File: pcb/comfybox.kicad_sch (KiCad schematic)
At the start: 20 parts, among them K1 SW_CHOC, K2 SW_CHOC, K3 SW_CHOC, K4 SW_CHOC, P1 SW_CHOC, P2 SW_CHOC, P3 SW_CHOC, P4 SW_CHOC

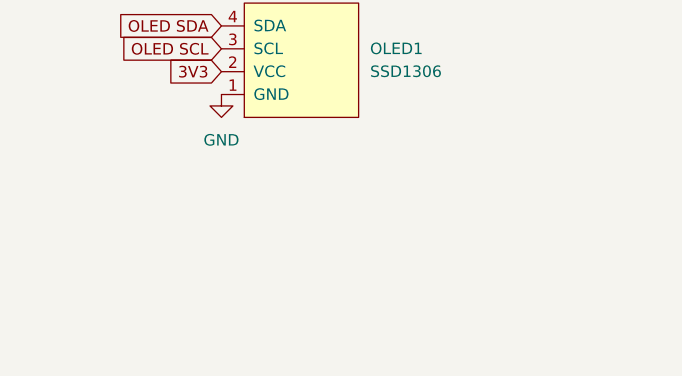
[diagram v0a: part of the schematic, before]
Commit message: add back oled
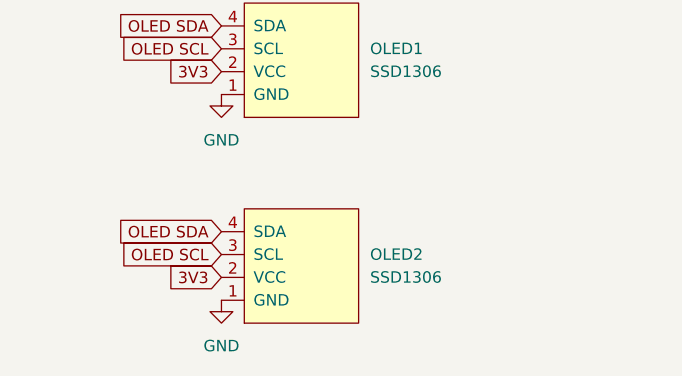
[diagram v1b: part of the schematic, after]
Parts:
- added OLED2: SSD1306, OLED:SSD1306-128x64_OLED, symbol SSD1306-128x64_OLED:SSD1306
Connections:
- net 3V3: now also OLED2.2 (VCC)
- net GND: now also OLED2.1 (GND)
- net OLED SCL: now also OLED2.3 (SCL)
- net OLED SDA: now also OLED2.4 (SDA)
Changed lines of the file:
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@@
+    )
+  )
+  (global_label "3V3" (shape input) (at 54.61 151.13 180) (fields_autoplaced)
+    (effects (font (size 1.27 1.27)) (justify right))
+    (property "Intersheetrefs" "${INTERSHEET_REFS}" (at 48.6893 151.2094 0)
+      (effects (font (size 1.27 1.27)) (justify right) hide)
     )
   )
@@
     )
   )
+  (global_label "OLED SCL" (shape input) (at 54.61 148.59 180) (fields_autoplaced)
+    (effects (font (size 1.27 1.27)) (justify right))
+    (property "Intersheetrefs" "${INTERSHEET_REFS}" (at 42.944 148.5106 0)
+      (effects (font (size 1.27 1.27)) (justify right) hide)
+    )
+  )
   (global_label "LEFT" (shape input) (at 115.57 72.39 270) (fields_autoplaced)
     (effects (font (size 1.27 1.27)) (justify right))
     (property "Intersheetrefs" "${INTERSHEET_REFS}" (at 115.4906 79.0364 90)
+      (effects (font (size 1.27 1.27)) (justify right) hide)
+    )
+  )
+  (global_label "OLED SDA" (shape input) (at 54.61 146.05 180) (fields_autoplaced)
+    (effects (font (size 1.27 1.27)) (justify right))
+    (property "Intersheetrefs" "${INTERSHEET_REFS}" (at 42.8836 145.9706 0)
       (effects (font (size 1.27 1.27)) (justify right) hide)
     )
@@
     )
   )
+  (symbol (lib_id "power:GND") (at 54.61 153.67 0) (unit 1)
+    (in_bom yes) (on_board yes) (dnp no) (fields_autoplaced)
+    (property "Reference" "#PWR03" (at 54.61 160.02 0)
+      (effects (font (size 1.27 1.27)) hide)
+    )
+    (property "Value" "GND" (at 54.61 158.75 0)
+      (effects (font (size 1.27 1.27)))
+    )
+    (property "Footprint" "" (at 54.61 153.67 0)
+      (effects (font (size 1.27 1.27)) hide)
+    )
+    (property "Datasheet" "" (at 54.61 153.67 0)
+      (effects (font (size 1.27 1.27)) hide)
+    )
+    (pin "1")
+    (instances
+      (project "comfybox"
+        (path "/9a77f188-2d2d-4d89-86c0-244b937205f9"
+          (reference "#PWR03") (unit 1)
+        )
+      )
+    )
+  )
   (symbol (lib_id "power:GND") (at 146.05 119.38 0) (unit 1)
     (in_bom yes) (on_board yes) (dnp no) (fields_autoplaced)
@@
         )
       )
+    )
+  )
+  (symbol (lib_id "SSD1306-128x64_OLED:SSD1306") (at 63.5 149.86 90) (unit 1)
+    (in_bom yes) (on_board yes) (dnp no) (fields_autoplaced)
+    (property "Reference" "OLED2" (at 71.12 148.5899 90)
+      (effects (font (size 1.27 1.27)) (justify right))
+    )
+    (property "Value" "SSD1306" (at 71.12 151.1299 90)
+      (effects (font (size 1.27 1.27)) (justify right))
+    )
+    (property "Footprint" "OLED:SSD1306-128x64_OLED" (at 57.15 149.86 0)
+      (effects (font (size 1.27 1.27)) hide)
+    )
+    (property "Datasheet" "" (at 57.15 149.86 0)
+      (effects (font (size 1.27 1.27)) hide)
+    )
+    (pin "1")
+    (pin "2")
+    (pin "3")
+    (pin "4")
+    (instances
+      (project "comfybox"
+        (path "/9a77f188-2d2d-4d89-86c0-244b937205f9"
+          (reference "OLED2") (unit 1)
+        )
+      )

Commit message: rework reversibility
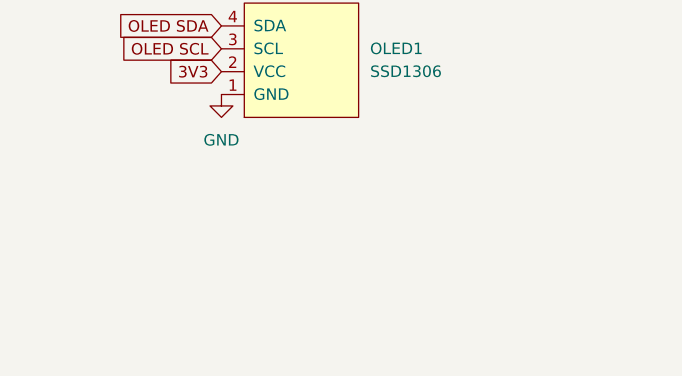
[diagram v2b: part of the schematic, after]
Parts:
- removed OLED2: SSD1306, OLED:SSD1306-128x64_OLED, symbol SSD1306-128x64_OLED:SSD1306
- OLED1: footprint OLED:SSD1306-128x64_OLED -> OLED:SSD1306-128x64_OLED_reversible
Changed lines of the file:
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@@
     (rev "0.1")
+  )
+  (wire (pts (xy 62.23 85.09) (xy 62.23 88.9))
+    (stroke (width 0) (type default))
   )
   (wire (pts (xy 64.77 50.8) (xy 64.77 52.07))
     (stroke (width 0) (type default))
   )
-  (wire (pts (xy 62.23 85.09) (xy 62.23 88.9))
-    (stroke (width 0) (type default))
-  )
   (wire (pts (xy 60.96 50.8) (xy 60.96 52.07))
     (stroke (width 0) (type default))
@@
     )
   )
-  (global_label "3V3" (shape input) (at 54.61 151.13 180) (fields_autoplaced)
-    (effects (font (size 1.27 1.27)) (justify right))
-    (property "Intersheetrefs" "${INTERSHEET_REFS}" (at 48.6893 151.2094 0)
-      (effects (font (size 1.27 1.27)) (justify right) hide)
-    )
-  )
   (global_label "K3" (shape input) (at 45.72 64.77 180) (fields_autoplaced)
     (effects (font (size 1.27 1.27)) (justify right))
@@
     )
   )
-  (global_label "OLED SCL" (shape input) (at 54.61 148.59 180) (fields_autoplaced)
-    (effects (font (size 1.27 1.27)) (justify right))
-    (property "Intersheetrefs" "${INTERSHEET_REFS}" (at 42.944 148.5106 0)
-      (effects (font (size 1.27 1.27)) (justify right) hide)
-    )
-  )
   (global_label "LEFT" (shape input) (at 115.57 72.39 270) (fields_autoplaced)
     (effects (font (size 1.27 1.27)) (justify right))
     (property "Intersheetrefs" "${INTERSHEET_REFS}" (at 115.4906 79.0364 90)
-      (effects (font (size 1.27 1.27)) (justify right) hide)
-    )
-  )
-  (global_label "OLED SDA" (shape input) (at 54.61 146.05 180) (fields_autoplaced)
-    (effects (font (size 1.27 1.27)) (justify right))
-    (property "Intersheetrefs" "${INTERSHEET_REFS}" (at 42.8836 145.9706 0)
       (effects (font (size 1.27 1.27)) (justify right) hide)
     )
@@
     )
   )
-  (symbol (lib_id "power:GND") (at 54.61 153.67 0) (unit 1)
-    (in_bom yes) (on_board yes) (dnp no) (fields_autoplaced)
-    (property "Reference" "#PWR03" (at 54.61 160.02 0)
-      (effects (font (size 1.27 1.27)) hide)
-    )
-    (property "Value" "GND" (at 54.61 158.75 0)
-      (effects (font (size 1.27 1.27)))
-    )
-    (property "Footprint" "" (at 54.61 153.67 0)
-      (effects (font (size 1.27 1.27)) hide)
-    )
-    (property "Datasheet" "" (at 54.61 153.67 0)
-      (effects (font (size 1.27 1.27)) hide)
-    )
-    (pin "1")
-    (instances
-      (project "comfybox"
-        (path "/9a77f188-2d2d-4d89-86c0-244b937205f9"
-          (reference "#PWR03") (unit 1)
-        )
-      )
-    )
-  )
   (symbol (lib_id "power:GND") (at 146.05 119.38 0) (unit 1)
     (in_bom yes) (on_board yes) (dnp no) (fields_autoplaced)
@@
       (effects (font (size 1.27 1.27)) (justify right))
     )
-    (property "Footprint" "OLED:SSD1306-128x64_OLED" (at 57.15 127 0)
+    (property "Footprint" "OLED:SSD1306-128x64_OLED_reversible" (at 57.15 127 0)
       (effects (font (size 1.27 1.27)) hide)
     )
@@
         )
       )
-    )
-  )
-  (symbol (lib_id "SSD1306-128x64_OLED:SSD1306") (at 63.5 149.86 90) (unit 1)
-    (in_bom yes) (on_board yes) (dnp no) (fields_autoplaced)
-    (property "Reference" "OLED2" (at 71.12 148.5899 90)
-      (effects (font (size 1.27 1.27)) (justify right))
-    )
-    (property "Value" "SSD1306" (at 71.12 151.1299 90)
-      (effects (font (size 1.27 1.27)) (justify right))
-    )
-    (property "Footprint" "OLED:SSD1306-128x64_OLED" (at 57.15 149.86 0)
-      (effects (font (size 1.27 1.27)) hide)
-    )
-    (property "Datasheet" "" (at 57.15 149.86 0)
-      (effects (font (size 1.27 1.27)) hide)
-    )
-    (pin "1")
-    (pin "2")
-    (pin "3")
-    (pin "4")
-    (instances
-      (project "comfybox"
-        (path "/9a77f188-2d2d-4d89-86c0-244b937205f9"
-          (reference "OLED2") (unit 1)
-        )
-      )

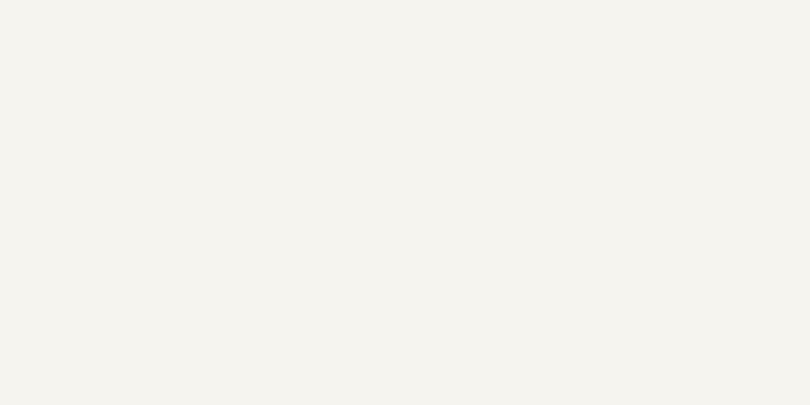
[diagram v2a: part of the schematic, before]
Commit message: add mounting holes
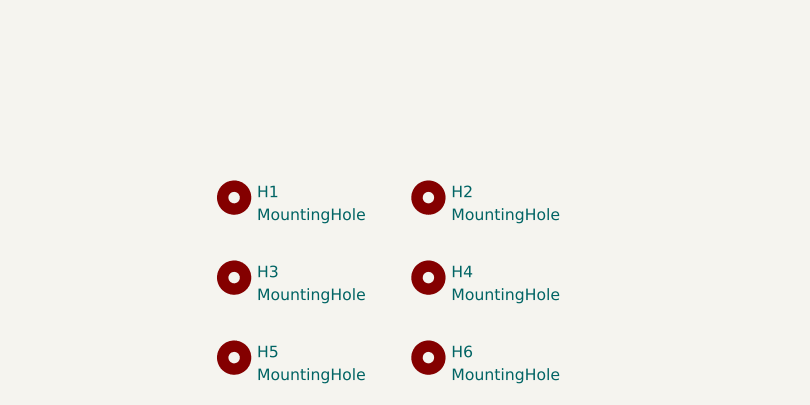
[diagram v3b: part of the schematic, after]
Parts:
- added H1, H2, H3, H4, H5, H6: MountingHole, MountingHole:MountingHole_4.3mm_M4, symbol Mechanical:MountingHole
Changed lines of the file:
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@@
+    )
+  )
+  (symbol (lib_id "Mechanical:MountingHole") (at 100.33 177.8 0) (unit 1)
+    (in_bom yes) (on_board yes) (dnp no) (fields_autoplaced)
+    (property "Reference" "H3" (at 102.87 177.165 0)
+      (effects (font (size 1.27 1.27)) (justify left))
+    )
+    (property "Value" "MountingHole" (at 102.87 179.705 0)
+      (effects (font (size 1.27 1.27)) (justify left))
+    )
+    (property "Footprint" "MountingHole:MountingHole_4.3mm_M4" (at 100.33 177.8 0)
+      (effects (font (size 1.27 1.27)) hide)
+    )
+    (property "Datasheet" "~" (at 100.33 177.8 0)
+      (effects (font (size 1.27 1.27)) hide)
+    )
+    (instances
+      (project "comfybox"
+        (path "/9a77f188-2d2d-4d89-86c0-244b937205f9"
+          (reference "H3") (unit 1)
+        )
+      )
     )
   )
@@
     )
   )
+  (symbol (lib_id "Mechanical:MountingHole") (at 100.33 168.91 0) (unit 1)
+    (in_bom yes) (on_board yes) (dnp no) (fields_autoplaced)
+    (property "Reference" "H1" (at 102.87 168.275 0)
+      (effects (font (size 1.27 1.27)) (justify left))
+    )
+    (property "Value" "MountingHole" (at 102.87 170.815 0)
+      (effects (font (size 1.27 1.27)) (justify left))
+    )
+    (property "Footprint" "MountingHole:MountingHole_4.3mm_M4" (at 100.33 168.91 0)
+      (effects (font (size 1.27 1.27)) hide)
+    )
+    (property "Datasheet" "~" (at 100.33 168.91 0)
+      (effects (font (size 1.27 1.27)) hide)
+    )
+    (instances
+      (project "comfybox"
+        (path "/9a77f188-2d2d-4d89-86c0-244b937205f9"
+          (reference "H1") (unit 1)
+        )
+      )
+    )
+  )
   (symbol (lib_id "power:GND") (at 146.05 38.1 0) (unit 1)
     (in_bom yes) (on_board yes) (dnp no) (fields_autoplaced)
@@
     )
   )
+  (symbol (lib_id "Mechanical:MountingHole") (at 100.33 186.69 0) (unit 1)
+    (in_bom yes) (on_board yes) (dnp no) (fields_autoplaced)
+    (property "Reference" "H5" (at 102.87 186.055 0)
+      (effects (font (size 1.27 1.27)) (justify left))
+    )
+    (property "Value" "MountingHole" (at 102.87 188.595 0)
+      (effects (font (size 1.27 1.27)) (justify left))
+    )
+    (property "Footprint" "MountingHole:MountingHole_4.3mm_M4" (at 100.33 186.69 0)
+      (effects (font (size 1.27 1.27)) hide)
+    )
+    (property "Datasheet" "~" (at 100.33 186.69 0)
+      (effects (font (size 1.27 1.27)) hide)
+    )
+    (instances
+      (project "comfybox"
+        (path "/9a77f188-2d2d-4d89-86c0-244b937205f9"
+          (reference "H5") (unit 1)
+        )
+      )
+    )
+  )
   (symbol (lib_id "power:GND") (at 186.69 72.39 0) (unit 1)
     (in_bom yes) (on_board yes) (dnp no) (fields_autoplaced)
@@
         (path "/9a77f188-2d2d-4d89-86c0-244b937205f9"
           (reference "OPT5") (unit 1)
+        )
+      )
+    )
+  )
+  (symbol (lib_id "Mechanical:MountingHole") (at 121.92 168.91 0) (unit 1)
+    (in_bom yes) (on_board yes) (dnp no) (fields_autoplaced)
+    (property "Reference" "H2" (at 124.46 168.275 0)
+      (effects (font (size 1.27 1.27)) (justify left))
+    )
+    (property "Value" "MountingHole" (at 124.46 170.815 0)
+      (effects (font (size 1.27 1.27)) (justify left))
+    )
+    (property "Footprint" "MountingHole:MountingHole_4.3mm_M4" (at 121.92 168.91 0)
+      (effects (font (size 1.27 1.27)) hide)
+    )
+    (property "Datasheet" "~" (at 121.92 168.91 0)
+      (effects (font (size 1.27 1.27)) hide)
+    )
+    (instances
+      (project "comfybox"
+        (path "/9a77f188-2d2d-4d89-86c0-244b937205f9"
+          (reference "H2") (unit 1)
         )
       )
@@
     )
   )
+  (symbol (lib_id "Mechanical:MountingHole") (at 121.92 177.8 0) (unit 1)
+    (in_bom yes) (on_board yes) (dnp no) (fields_autoplaced)
+    (property "Reference" "H4" (at 124.46 177.165 0)
+      (effects (font (size 1.27 1.27)) (justify left))
+    )
+    (property "Value" "MountingHole" (at 124.46 179.705 0)
+      (effects (font (size 1.27 1.27)) (justify left))
+    )
+    (property "Footprint" "MountingHole:MountingHole_4.3mm_M4" (at 121.92 177.8 0)
+      (effects (font (size 1.27 1.27)) hide)
+    )
+    (property "Datasheet" "~" (at 121.92 177.8 0)
+      (effects (font (size 1.27 1.27)) hide)
+    )
+    (instances
+      (project "comfybox"
+        (path "/9a77f188-2d2d-4d89-86c0-244b937205f9"
+          (reference "H4") (unit 1)
+        )
+      )
+    )
+  )
   (symbol (lib_id "power:GND") (at 166.37 38.1 0) (unit 1)
     (in_bom yes) (on_board yes) (dnp no) (fields_autoplaced)
@@
         )
       )
+    )
+  )
+  (symbol (lib_id "Mechanical:MountingHole") (at 121.92 186.69 0) (unit 1)
+    (in_bom yes) (on_board yes) (dnp no) (fields_autoplaced)
+    (property "Reference" "H6" (at 124.46 186.055 0)
+      (effects (font (size 1.27 1.27)) (justify left))
+    )
+    (property "Value" "MountingHole" (at 124.46 188.595 0)
+      (effects (font (size 1.27 1.27)) (justify left))
+    )
+    (property "Footprint" "MountingHole:MountingHole_4.3mm_M4" (at 121.92 186.69 0)
+      (effects (font (size 1.27 1.27)) hide)
+    )
+    (property "Datasheet" "~" (at 121.92 186.69 0)
+      (effects (font (size 1.27 1.27)) hide)
+    )
+    (instances
+      (project "comfybox"
+        (path "/9a77f188-2d2d-4d89-86c0-244b937205f9"
+          (reference "H6") (unit 1)
+        )
+      )

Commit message: update footprints
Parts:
- DOWN1, K1, K2, K3, K4, LEFT1, P1, P2, P3, P4, RIGHT1, UP1, UP2: footprint Switch:Kailh_PG1350_Gateron_KS33_MX_reversible -> Switch:Kailh_CPG1353_Gateron_KS33_MX_reversible
- H1, H2, H3, H4, H5, H6: footprint MountingHole:MountingHole_4.3mm_M4 -> MountingHole:MountingHole_4mm
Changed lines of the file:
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@@
       (effects (font (size 1.27 1.27)))
     )
-    (property "Footprint" "Switch:Kailh_PG1350_Gateron_KS33_MX_reversible" (at 120.65 67.31 0)
+    (property "Footprint" "Switch:Kailh_CPG1353_Gateron_KS33_MX_reversible" (at 120.65 67.31 0)
       (effects (font (size 1.27 1.27)) hide)
     )
@@
       (effects (font (size 1.27 1.27)))
     )
-    (property "Footprint" "Switch:Kailh_PG1350_Gateron_KS33_MX_reversible" (at 181.61 114.3 0)
+    (property "Footprint" "Switch:Kailh_CPG1353_Gateron_KS33_MX_reversible" (at 181.61 114.3 0)
       (effects (font (size 1.27 1.27)) hide)
     )
@@
       (effects (font (size 1.27 1.27)))
     )
-    (property "Footprint" "Switch:Kailh_PG1350_Gateron_KS33_MX_reversible" (at 140.97 114.3 0)
+    (property "Footprint" "Switch:Kailh_CPG1353_Gateron_KS33_MX_reversible" (at 140.97 114.3 0)
       (effects (font (size 1.27 1.27)) hide)
     )
@@
       (effects (font (size 1.27 1.27)) (justify left))
     )
-    (property "Footprint" "MountingHole:MountingHole_4.3mm_M4" (at 100.33 177.8 0)
+    (property "Footprint" "MountingHole:MountingHole_4mm" (at 100.33 177.8 0)
       (effects (font (size 1.27 1.27)) hide)
     )
@@
       (effects (font (size 1.27 1.27)))
     )
-    (property "Footprint" "Switch:Kailh_PG1350_Gateron_KS33_MX_reversible" (at 201.93 67.31 0)
+    (property "Footprint" "Switch:Kailh_CPG1353_Gateron_KS33_MX_reversible" (at 201.93 67.31 0)
       (effects (font (size 1.27 1.27)) hide)
     )
@@
       (effects (font (size 1.27 1.27)) (justify left))
     )
-    (property "Footprint" "MountingHole:MountingHole_4.3mm_M4" (at 100.33 168.91 0)
+    (property "Footprint" "MountingHole:MountingHole_4mm" (at 100.33 168.91 0)
       (effects (font (size 1.27 1.27)) hide)
     )
@@
       (effects (font (size 1.27 1.27)) (justify left))
     )
-    (property "Footprint" "MountingHole:MountingHole_4.3mm_M4" (at 100.33 186.69 0)
+    (property "Footprint" "MountingHole:MountingHole_4mm" (at 100.33 186.69 0)
       (effects (font (size 1.27 1.27)) hide)
     )
@@
       (effects (font (size 1.27 1.27)) (justify left))
     )
-    (property "Footprint" "MountingHole:MountingHole_4.3mm_M4" (at 121.92 168.91 0)
+    (property "Footprint" "MountingHole:MountingHole_4mm" (at 121.92 168.91 0)
       (effects (font (size 1.27 1.27)) hide)
     )
@@
       (effects (font (size 1.27 1.27)))
     )
-    (property "Footprint" "Switch:Kailh_PG1350_Gateron_KS33_MX_reversible" (at 120.65 92.71 0)
+    (property "Footprint" "Switch:Kailh_CPG1353_Gateron_KS33_MX_reversible" (at 120.65 92.71 0)
       (effects (font (size 1.27 1.27)) hide)
     )
@@
       (effects (font (size 1.27 1.27)))
     )
-    (property "Footprint" "Switch:Kailh_PG1350_Gateron_KS33_MX_reversible" (at 161.29 114.3 0)
+    (property "Footprint" "Switch:Kailh_CPG1353_Gateron_KS33_MX_reversible" (at 161.29 114.3 0)
       (effects (font (size 1.27 1.27)) hide)
     )
@@
       (effects (font (size 1.27 1.27)))
     )
-    (property "Footprint" "Switch:Kailh_PG1350_Gateron_KS33_MX_reversible" (at 181.61 92.71 0)
+    (property "Footprint" "Switch:Kailh_CPG1353_Gateron_KS33_MX_reversible" (at 181.61 92.71 0)
       (effects (font (size 1.27 1.27)) hide)
     )
@@
       (effects (font (size 1.27 1.27)))
     )
-    (property "Footprint" "Switch:Kailh_PG1350_Gateron_KS33_MX_reversible" (at 161.29 92.71 0)
+    (property "Footprint" "Switch:Kailh_CPG1353_Gateron_KS33_MX_reversible" (at 161.29 92.71 0)
       (effects (font (size 1.27 1.27)) hide)
     )
@@
       (effects (font (size 1.27 1.27)))
     )
-    (property "Footprint" "Switch:Kailh_PG1350_Gateron_KS33_MX_reversible" (at 140.97 67.31 0)
+    (property "Footprint" "Switch:Kailh_CPG1353_Gateron_KS33_MX_reversible" (at 140.97 67.31 0)
       (effects (font (size 1.27 1.27)) hide)
     )
@@
       (effects (font (size 1.27 1.27)))
     )
-    (property "Footprint" "Switch:Kailh_PG1350_Gateron_KS33_MX_reversible" (at 120.65 114.3 0)
+    (property "Footprint" "Switch:Kailh_CPG1353_Gateron_KS33_MX_reversible" (at 120.65 114.3 0)
       (effects (font (size 1.27 1.27)) hide)
     )
@@
       (effects (font (size 1.27 1.27)) (justify left))
     )
-    (property "Footprint" "MountingHole:MountingHole_4.3mm_M4" (at 121.92 177.8 0)
+    (property "Footprint" "MountingHole:MountingHole_4mm" (at 121.92 177.8 0)
       (effects (font (size 1.27 1.27)) hide)
     )
@@
       (effects (font (size 1.27 1.27)))
     )
-    (property "Footprint" "Switch:Kailh_PG1350_Gateron_KS33_MX_reversible" (at 140.97 92.71 0)
+    (property "Footprint" "Switch:Kailh_CPG1353_Gateron_KS33_MX_reversible" (at 140.97 92.71 0)
       (effects (font (size 1.27 1.27)) hide)
     )
@@
       (effects (font (size 1.27 1.27)))
     )
-    (property "Footprint" "Switch:Kailh_PG1350_Gateron_KS33_MX_reversible" (at 181.61 67.31 0)
+    (property "Footprint" "Switch:Kailh_CPG1353_Gateron_KS33_MX_reversible" (at 181.61 67.31 0)
       (effects (font (size 1.27 1.27)) hide)
     )
@@
       (effects (font (size 1.27 1.27)))
     )
-    (property "Footprint" "Switch:Kailh_PG1350_Gateron_KS33_MX_reversible" (at 161.29 67.31 0)
+    (property "Footprint" "Switch:Kailh_CPG1353_Gateron_KS33_MX_reversible" (at 161.29 67.31 0)
       (effects (font (size 1.27 1.27)) hide)
     )
@@
       (effects (font (size 1.27 1.27)) (justify left))
     )
-    (property "Footprint" "MountingHole:MountingHole_4.3mm_M4" (at 121.92 186.69 0)
-      (effects (font (size 1.27 1.27)) hide)
-    )
+    (property "Footprint" "MountingHole:MountingHole_4mm" (at 121.92 186.69 0)
+      (effects (font (size 1.27 1.27)) hide)
+    )
